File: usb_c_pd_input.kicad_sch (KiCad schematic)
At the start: 23 parts, among them J1 USB_C_Receptacle, U3 STUSB4500QTR, U4 STL6P3LLH6

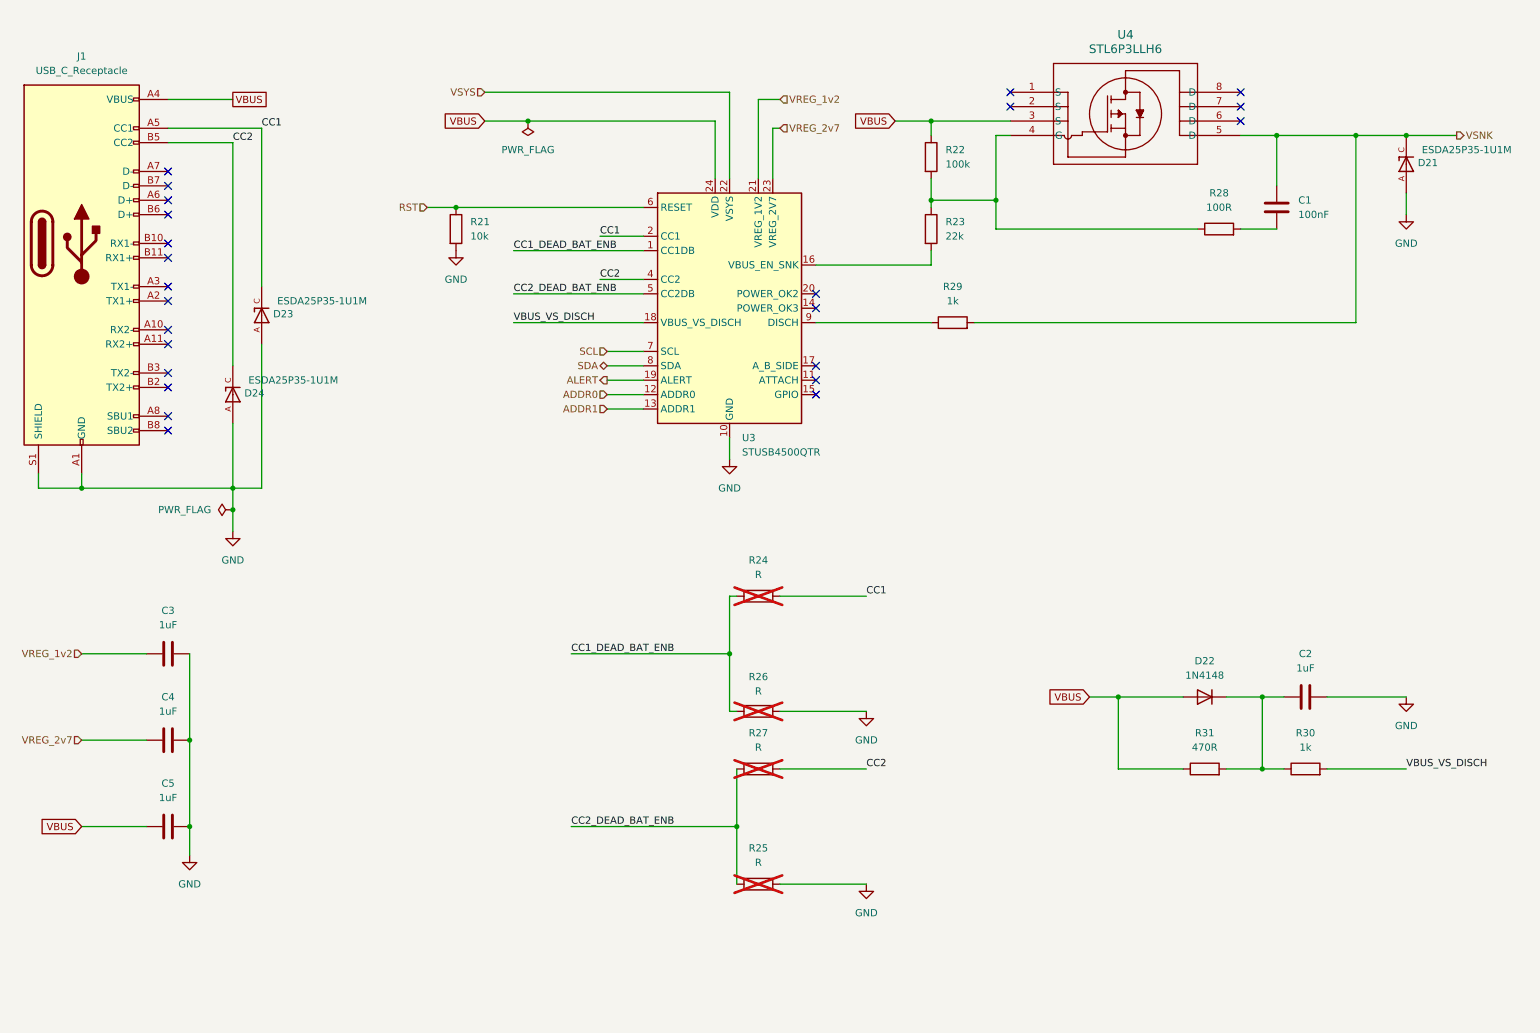
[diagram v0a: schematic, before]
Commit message: Fixup resistor values
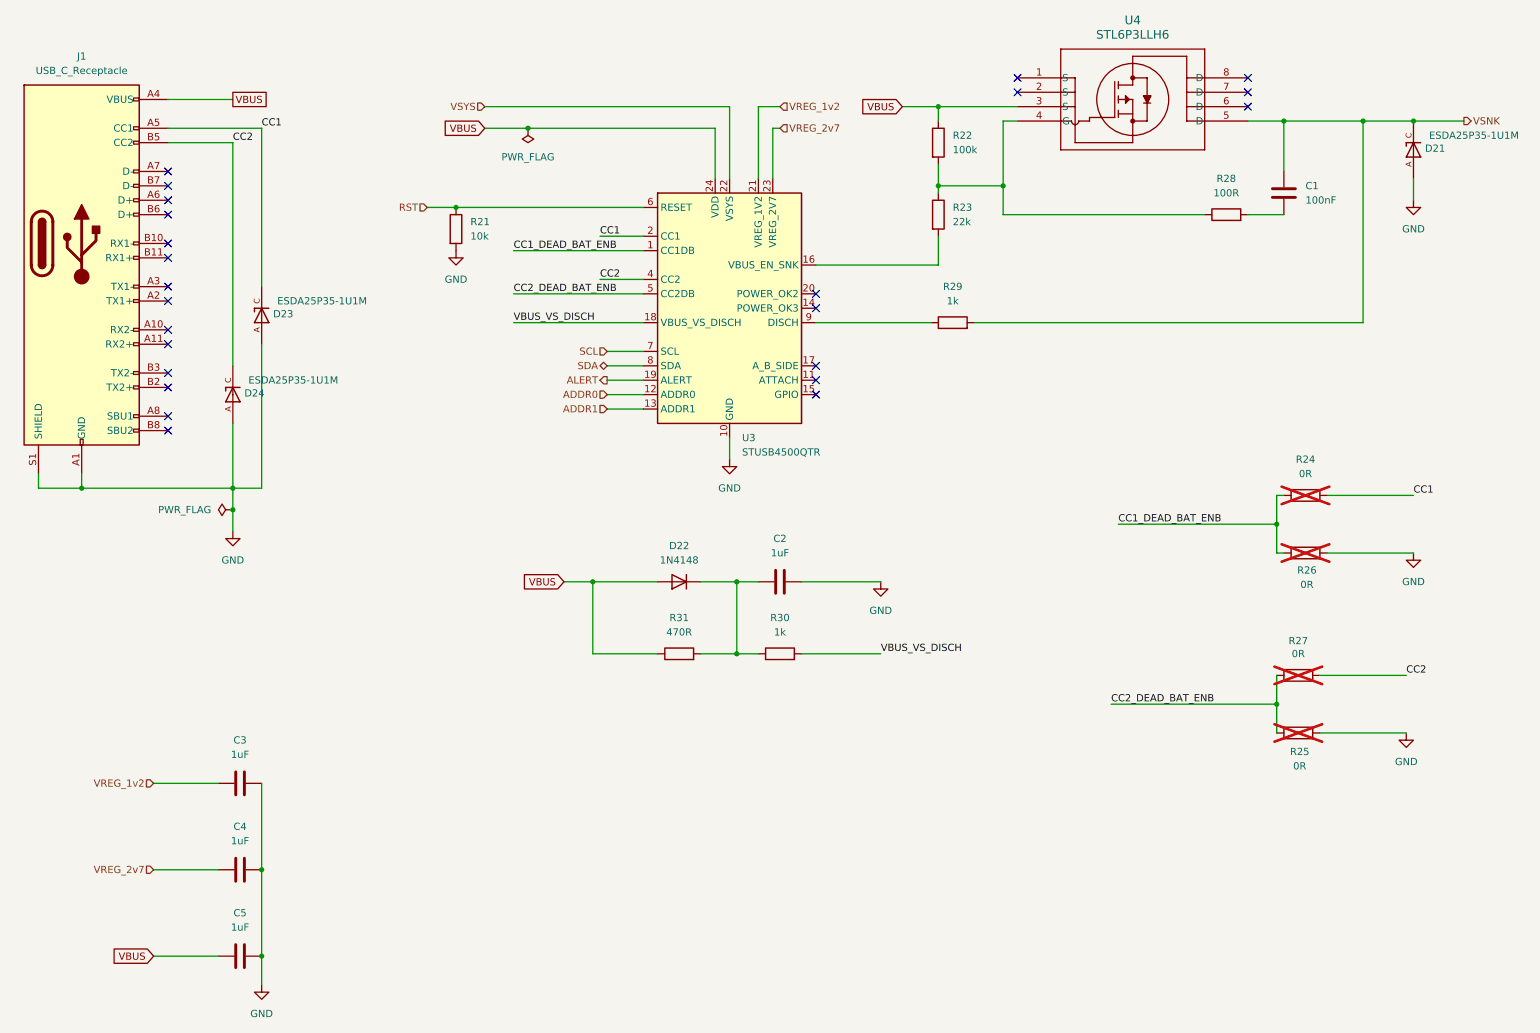
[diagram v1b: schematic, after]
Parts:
- R24, R25, R26, R27: value R -> 0R
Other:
- moved on the sheet: C1, C2, C3, C4, C5, D21, D22, R22, R23, R24, R25, R26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
